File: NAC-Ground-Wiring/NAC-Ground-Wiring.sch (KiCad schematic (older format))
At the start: 6 parts

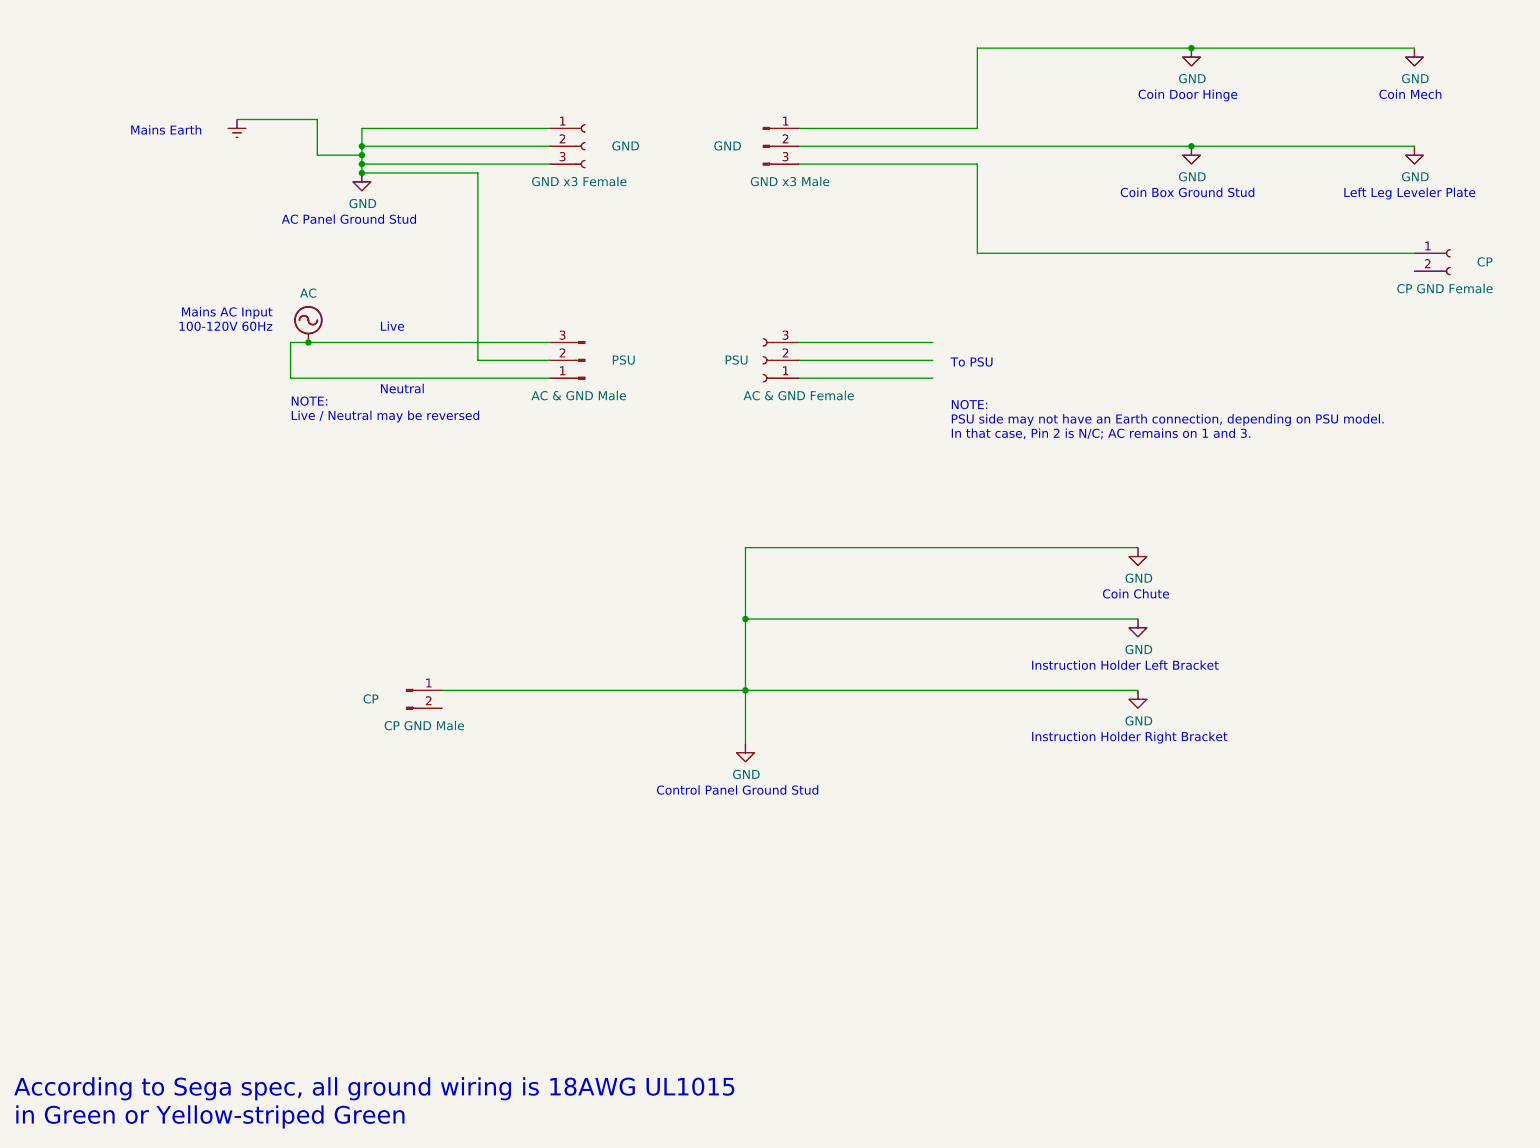
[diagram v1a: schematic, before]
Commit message: Updates to show CP Hinge connections
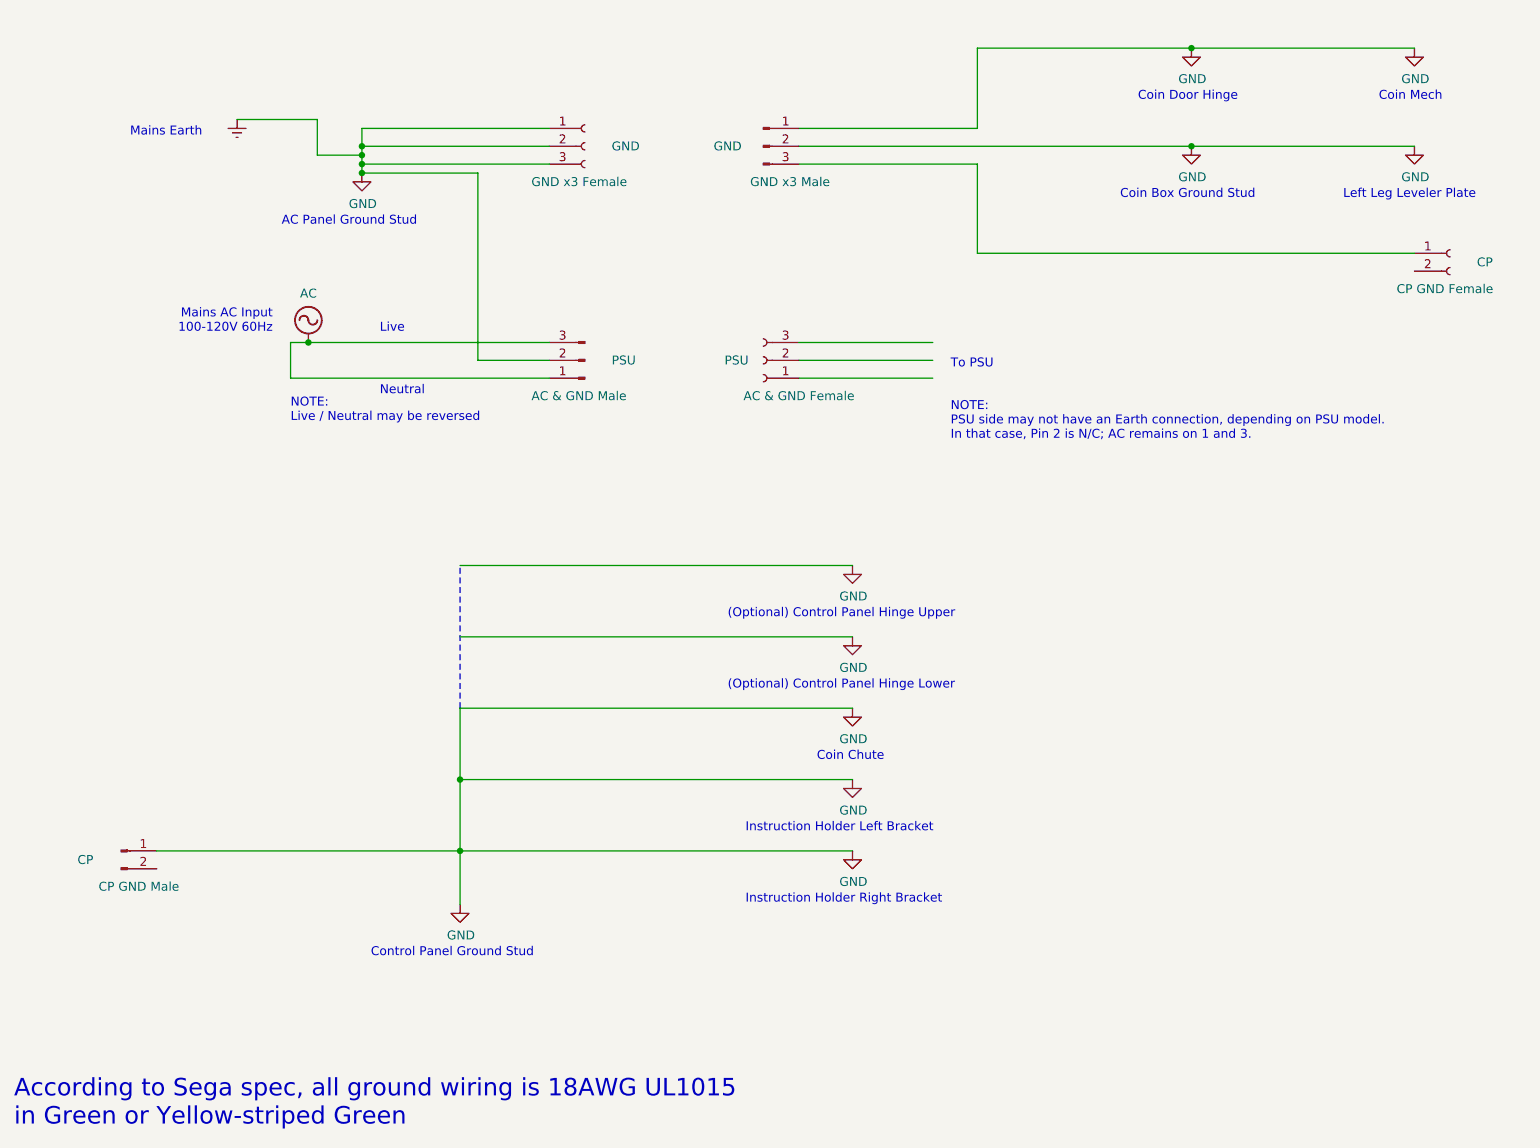
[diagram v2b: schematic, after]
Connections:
- wire segments 36 -> 38
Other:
- note added: "(Optional) Control Panel Hinge Lower"
- note added: "(Optional) Control Panel Hinge Upper"
- moved on the sheet: CP
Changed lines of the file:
@@
 encoding utf-8
 Sheet 1 1
-Title "New Astro City Ground Wiring"
+Title "Astro/New Astro City Ground Wiring"
 Date "2020-12-21"
-Rev "1.1"
+Rev "1.1b"
 Comp "Softdrink 117"
 Comment1 ""
-Comment2 "Updated based on official Sega wiring diagrams."
-Comment3 "Diagram of earth ground wiring connections in a Sega New Astro City arcade cabinet."
+Comment2 "New Astro City arcade cabinet. Updated based on official Sega wiring diagrams."
+Comment3 "Diagram of earth ground wiring connections in a Sega Astro City or early model "
 Comment4 ""
 $EndDescr
@@
 L power:GND #PWR?
 U 1 1 5FBDAFC3
-P 4800 5450
-F 0 "#PWR?" H 4800 5200 50  0001 C CNN
-F 1 "GND" H 4805 5277 50  0000 C CNN
-F 2 "" H 4800 5450 50  0001 C CNN
-F 3 "" H 4800 5450 50  0001 C CNN
-	1    4800 5450
+P 3200 6350
+F 0 "#PWR?" H 3200 6100 50  0001 C CNN
+F 1 "GND" H 3205 6177 50  0000 C CNN
+F 2 "" H 3200 6350 50  0001 C CNN
+F 3 "" H 3200 6350 50  0001 C CNN
+	1    3200 6350
 	1    0    0    -1
 $EndComp
@@
 L power:GND #PWR?
 U 1 1 5FBDB307
-P 7000 4350
-F 0 "#PWR?" H 7000 4100 50  0001 C CNN
-F 1 "GND" H 7005 4177 50  0000 C CNN
-F 2 "" H 7000 4350 50  0001 C CNN
-F 3 "" H 7000 4350 50  0001 C CNN
-	1    7000 4350
+P 5400 5250
+F 0 "#PWR?" H 5400 5000 50  0001 C CNN
+F 1 "GND" H 5405 5077 50  0000 C CNN
+F 2 "" H 5400 5250 50  0001 C CNN
+F 3 "" H 5400 5250 50  0001 C CNN
+	1    5400 5250
 	1    0    0    -1
 $EndComp
@@
 L power:GND #PWR?
 U 1 1 5FBDB90D
-P 7000 4750
-F 0 "#PWR?" H 7000 4500 50  0001 C CNN
-F 1 "GND" H 7005 4577 50  0000 C CNN
-F 2 "" H 7000 4750 50  0001 C CNN
-F 3 "" H 7000 4750 50  0001 C CNN
-	1    7000 4750
+P 5400 5650
+F 0 "#PWR?" H 5400 5400 50  0001 C CNN
+F 1 "GND" H 5405 5477 50  0000 C CNN
+F 2 "" H 5400 5650 50  0001 C CNN
+F 3 "" H 5400 5650 50  0001 C CNN
+	1    5400 5650
 	1    0    0    -1
 $EndComp
@@
 L power:GND #PWR?
 U 1 1 5FBDBD8E
-P 7000 5150
-F 0 "#PWR?" H 7000 4900 50  0001 C CNN
-F 1 "GND" H 7005 4977 50  0000 C CNN
-F 2 "" H 7000 5150 50  0001 C CNN
-F 3 "" H 7000 5150 50  0001 C CNN
-	1    7000 5150
-	1    0    0    -1
-$EndComp
-Text Notes 6800 4650 0    50   ~ 0
+P 5400 6050
+F 0 "#PWR?" H 5400 5800 50  0001 C CNN
+F 1 "GND" H 5405 5877 50  0000 C CNN
+F 2 "" H 5400 6050 50  0001 C CNN
+F 3 "" H 5400 6050 50  0001 C CNN
+	1    5400 6050
+	1    0    0    -1
+$EndComp
+Text Notes 5200 5550 0    50   ~ 0
 Coin Chute
-Text Notes 6400 5050 0    50   ~ 0
+Text Notes 4800 5950 0    50   ~ 0
 Instruction Holder Left Bracket
-Text Notes 6400 5450 0    50   ~ 0
+Text Notes 4800 6350 0    50   ~ 0
 Instruction Holder Right Bracket
-Text Notes 4300 5750 0    50   ~ 0
+Text Notes 2700 6650 0    50   ~ 0
 Control Panel Ground Stud
 Wire Wire Line
-	4800 5450 4800 5150
-Wire Wire Line
-	4800 4350 7000 4350
-Wire Wire Line
-	7000 4750 4800 4750
-Connection ~ 4800 4750
-Wire Wire Line
-	4800 4750 4800 4350
-Wire Wire Line
-	7000 5150 4800 5150
-Connection ~ 4800 5150
-Wire Wire Line
-	4800 5150 4800 4750
+	3200 6350 3200 6050
+Wire Wire Line
+	5400 5650 3200 5650
+Wire Wire Line
+	5400 6050 3200 6050
+Connection ~ 3200 6050
+Wire Wire Line
+	3200 6050 3200 5650
 Wire Wire Line
 	2650 2000 2650 2100
@@
 L Connector:Conn_01x02_Male CP
 U 1 1 5FE1C0D0
-P 2900 5150
-F 0 "CP" H 2700 5100 50  0000 C CNN
-F 1 "CP GND Male" H 3000 4950 50  0000 C CNN
-F 2 "" H 2900 5150 50  0001 C CNN
-F 3 "~" H 2900 5150 50  0001 C CNN
-	1    2900 5150
-	1    0    0    -1
-$EndComp
-Wire Wire Line
-	3100 5150 4800 5150
+P 1300 6050
+F 0 "CP" H 1100 6000 50  0000 C CNN
+F 1 "CP GND Male" H 1400 5850 50  0000 C CNN
+F 2 "" H 1300 6050 50  0001 C CNN
+F 3 "~" H 1300 6050 50  0001 C CNN
+	1    1300 6050
+	1    0    0    -1
+$EndComp
+Wire Wire Line
+	1500 6050 3200 6050
 Text Notes 2250 3650 0    50   ~ 0
 NOTE:\nLive / Neutral may be reversed
@@
 Text Notes 700  7600 0    98   ~ 0
 According to Sega spec, all ground wiring is 18AWG UL1015 \nin Green or Yellow-striped Green
+$Comp
+L power:GND #PWR?
+U 1 1 5FE325FF
+P 5400 4850
+F 0 "#PWR?" H 5400 4600 50  0001 C CNN
+F 1 "GND" H 5405 4677 50  0000 C CNN
+F 2 "" H 5400 4850 50  0001 C CNN
+F 3 "" H 5400 4850 50  0001 C CNN
+	1    5400 4850
+	1    0    0    -1
+$EndComp
+$Comp
+L power:GND #PWR?
+U 1 1 5FE32C52
+P 5400 4450
+F 0 "#PWR?" H 5400 4200 50  0001 C CNN
+F 1 "GND" H 5405 4277 50  0000 C CNN
+F 2 "" H 5400 4450 50  0001 C CNN
+F 3 "" H 5400 4450 50  0001 C CNN
+	1    5400 4450
+	1    0    0    -1
+$EndComp
+Connection ~ 3200 5650
+Wire Wire Line
+	3200 4850 5400 4850
+Wire Wire Line
+	5400 4450 3200 4450
+Wire Wire Line
+	3200 5650 3200 5250
+Wire Wire Line
+	3200 5250 5400 5250
+Wire Notes Line
+	3200 5250 3200 4450
+Text Notes 4700 4750 0    50   ~ 0
+(Optional) Control Panel Hinge Upper
+Text Notes 4700 5150 0    50   ~ 0
+(Optional) Control Panel Hinge Lower
 $EndSCHEMATC
